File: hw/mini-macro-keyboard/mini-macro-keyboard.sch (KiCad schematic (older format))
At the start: 11 parts

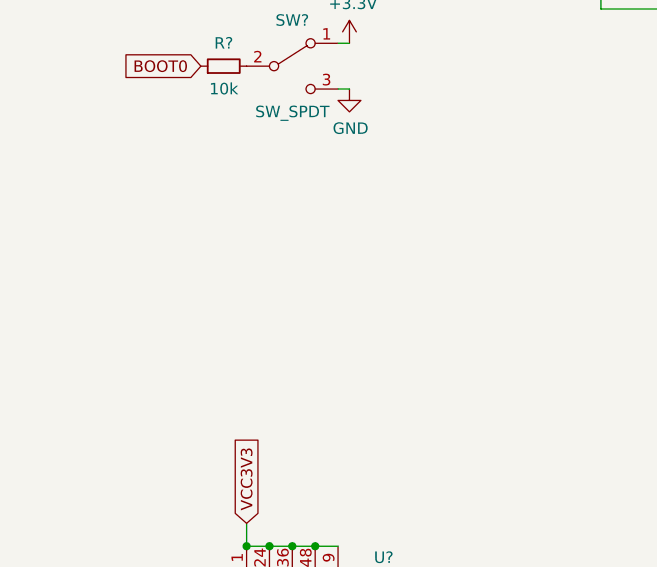
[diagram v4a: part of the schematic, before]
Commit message: feat(hw): add crystal to the schematic
Signed-off-by: Ivan Kovalenko <s1ckretbox@gmail.com>
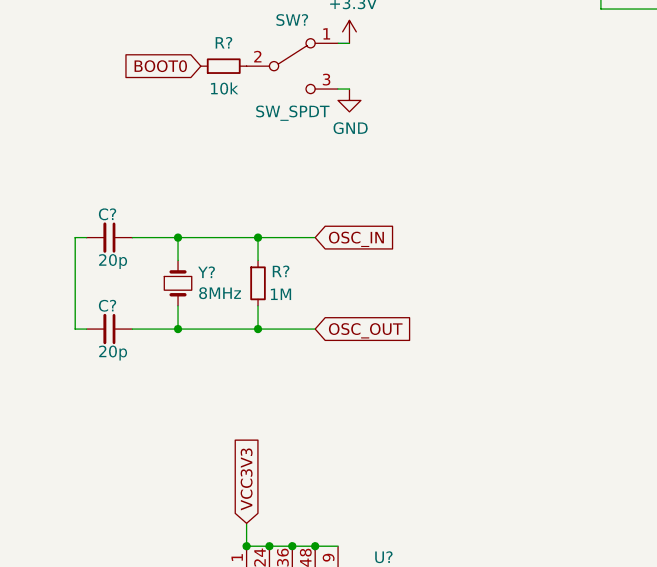
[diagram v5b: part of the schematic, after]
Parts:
- added C? (x2): 20p, symbol Device:C_Small
- added R?: 1M, symbol Device:R_Small
- added Y?: 8MHz, symbol Device:Crystal_Small
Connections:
- net OSC_IN: now also C?.1, R?.1, Y?.1
- net OSC_OUT: now also C?.1, R?.2, Y?.2
- new net: C?.2, C?.2
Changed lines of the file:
@@
 Text GLabel 3700 1200 1    50   Input ~ 0
 VCC3V3
-$Comp
-L Device:R_Small R?
-U 1 1 5FFE7355
-P 3700 1350
-F 0 "R?" V 3800 1350 50  0000 C CNN
-F 1 "10k" V 3600 1350 50  0000 C CNN
-F 2 "" H 3700 1350 50  0001 C CNN
-F 3 "~" H 3700 1350 50  0001 C CNN
-	1    3700 1350
-	1    0    0    -1
-$EndComp
 Wire Wire Line
 	3700 1250 3700 1200
@@
 Text GLabel 1200 4950 0    50   Input ~ 0
 OSC_IN
-Text GLabel 1200 5050 0    50   Input ~ 0
-OSC_OUT
 Text GLabel 2500 6950 2    50   Input ~ 0
 SWDIO
@@
 NoConn ~ 1200 5350
 NoConn ~ 1200 5250
+Text GLabel 1200 5050 0    50   Input ~ 0
+OSC_OUT
+$Comp
+L Device:Crystal_Small Y?
+U 1 1 6000CA22
+P 1400 3200
+F 0 "Y?" V 1354 3288 50  0000 L CNN
+F 1 "8MHz" V 1445 3288 50  0000 L CNN
+F 2 "" H 1400 3200 50  0001 C CNN
+F 3 "~" H 1400 3200 50  0001 C CNN
+	1    1400 3200
+	0    1    1    0
+$EndComp
+$Comp
+L Device:C_Small C?
+U 1 1 6000E4D6
+P 1100 3000
+F 0 "C?" V 1000 2950 50  0000 L CNN
+F 1 "20p" V 1200 2950 50  0000 L CNN
+F 2 "" H 1100 3000 50  0001 C CNN
+F 3 "~" H 1100 3000 50  0001 C CNN
+	1    1100 3000
+	0    1    1    0
+$EndComp
+$Comp
+L Device:C_Small C?
+U 1 1 6000EB9A
+P 1100 3400
+F 0 "C?" V 1000 3350 50  0000 L CNN
+F 1 "20p" V 1200 3350 50  0000 L CNN
+F 2 "" H 1100 3400 50  0001 C CNN
+F 3 "~" H 1100 3400 50  0001 C CNN
+	1    1100 3400
+	0    1    1    0
+$EndComp
+$Comp
+L Device:R_Small R?
+U 1 1 5FFE7355
+P 3700 1350
+F 0 "R?" V 3800 1350 50  0000 C CNN
+F 1 "10k" V 3600 1350 50  0000 C CNN
+F 2 "" H 3700 1350 50  0001 C CNN
+F 3 "~" H 3700 1350 50  0001 C CNN
+	1    3700 1350
+	1    0    0    -1
+$EndComp
+$Comp
+L Device:R_Small R?
+U 1 1 60011E97
+P 1750 3200
+F 0 "R?" H 1850 3250 50  0000 C CNN
+F 1 "1M" H 1850 3150 50  0000 C CNN
+F 2 "" H 1750 3200 50  0001 C CNN
+F 3 "~" H 1750 3200 50  0001 C CNN
+	1    1750 3200
+	1    0    0    -1
+$EndComp
+Wire Wire Line
+	1000 3000 950  3000
+Wire Wire Line
+	950  3000 950  3400
+Wire Wire Line
+	950  3400 1000 3400
+Wire Wire Line
+	1200 3000 1400 3000
+Wire Wire Line
+	1400 3000 1400 3100
+Wire Wire Line
+	1400 3300 1400 3400
+Wire Wire Line
+	1400 3400 1200 3400
+Connection ~ 1400 3000
+Connection ~ 1400 3400
+Text GLabel 2000 3000 2    50   Input ~ 0
+OSC_IN
+Text GLabel 2000 3400 2    50   Input ~ 0
+OSC_OUT
+Wire Wire Line
+	1400 3400 1750 3400
+Wire Wire Line
+	1400 3000 1750 3000
+Wire Wire Line
+	1750 3100 1750 3000
+Connection ~ 1750 3000
+Wire Wire Line
+	1750 3000 2000 3000
+Wire Wire Line
+	1750 3300 1750 3400
+Connection ~ 1750 3400
+Wire Wire Line
+	1750 3400 2000 3400
 $EndSCHEMATC

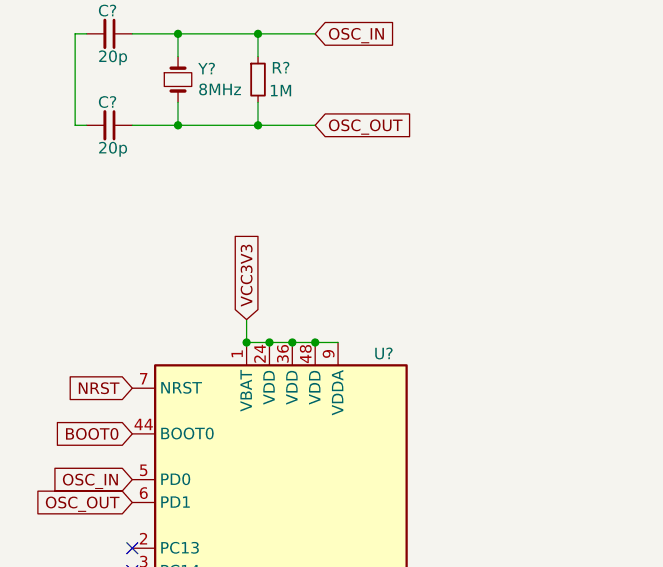
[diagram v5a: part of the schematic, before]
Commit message: fix(hw): remove VBAT connection
Signed-off-by: Ivan Kovalenko <s1ckretbox@gmail.com>
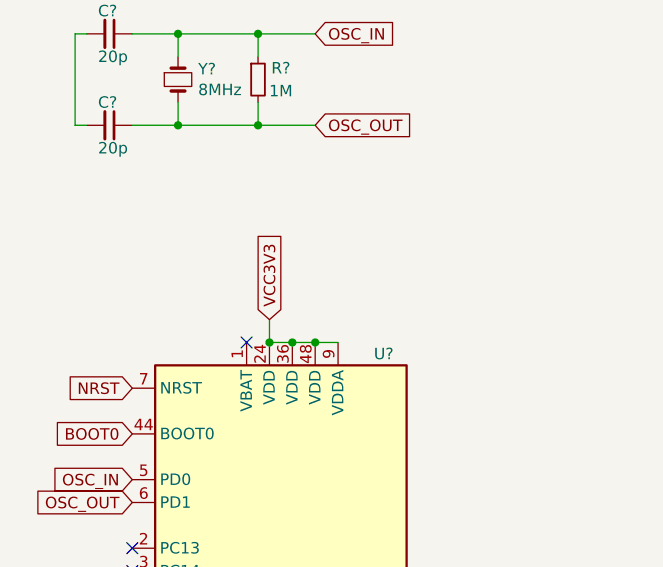
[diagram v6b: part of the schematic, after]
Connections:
- net +3V3: no longer U?.1 (VBAT)
- no-connect marks 24 -> 25
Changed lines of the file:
@@
 Wire Wire Line
 	1700 7350 1700 7450
-Text GLabel 1700 4250 1    50   Input ~ 0
+Text GLabel 1800 4250 1    50   Input ~ 0
 VCC3V3
 Text GLabel 1150 1100 0    50   Input ~ 0
 VCC3V3
-Wire Wire Line
-	1700 4250 1700 4350
 $Comp
 L Device:C_Small C?
@@
 	0    -1   -1   0
 $EndComp
-Connection ~ 1700 4350
 Connection ~ 2000 4350
 Wire Wire Line
@@
 	1900 4350 2000 4350
 Connection ~ 1900 4350
-Connection ~ 1800 4350
 Wire Wire Line
 	1800 4350 1900 4350
-Wire Wire Line
-	1700 4350 1800 4350
 Wire Wire Line
 	1900 7350 2000 7350
@@
 Wire Wire Line
 	1750 3400 2000 3400
+Wire Wire Line
+	1800 4250 1800 4350
+Connection ~ 1800 4350
+NoConn ~ 1700 4350
 $EndSCHEMATC

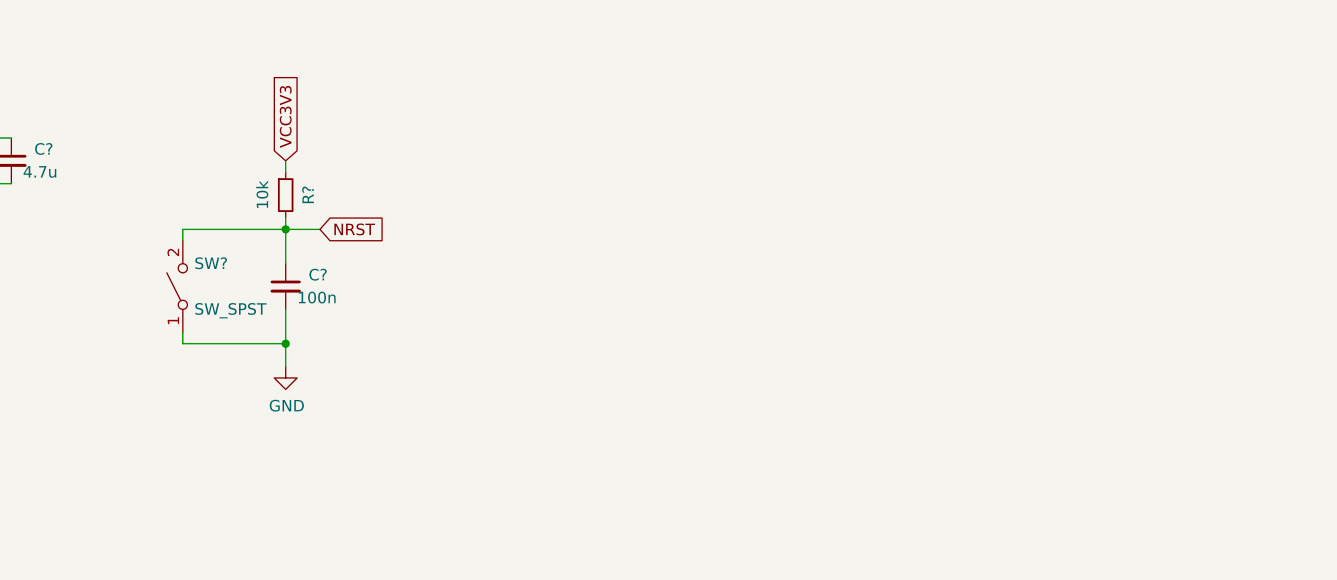
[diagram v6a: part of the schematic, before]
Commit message: feat(hw): add usblc6 protection
Signed-off-by: Ivan Kovalenko <s1ckretbox@gmail.com>
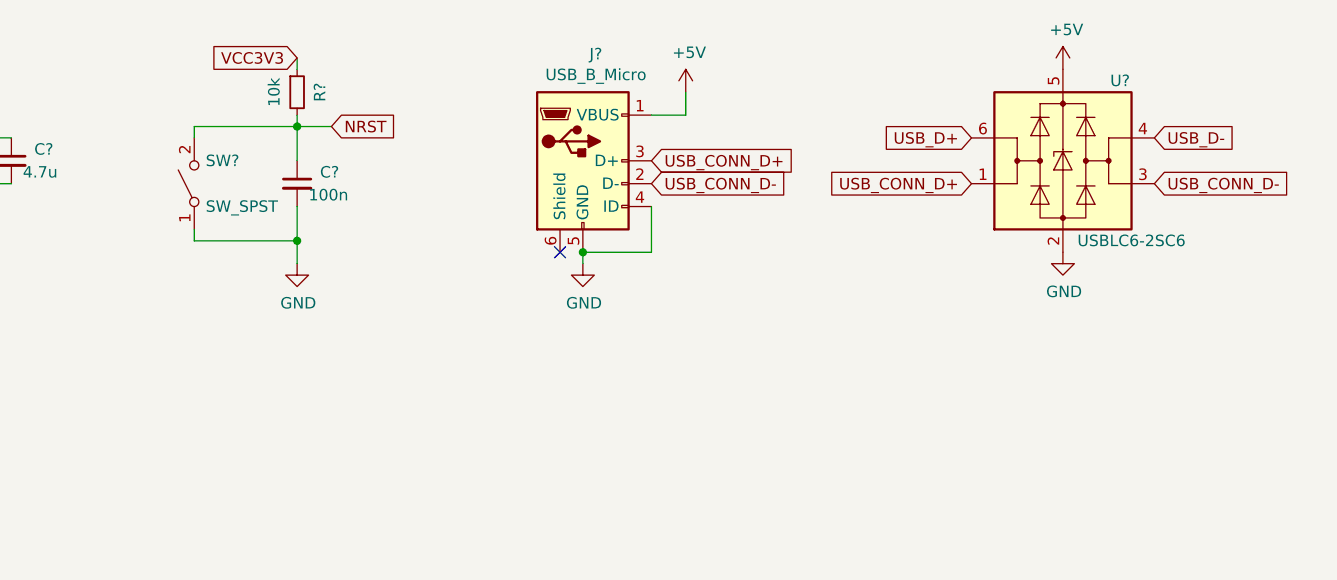
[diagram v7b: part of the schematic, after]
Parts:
- added J?: USB_B_Micro, symbol Connector:USB_B_Micro
- added U?: USBLC6-2SC6, Package_TO_SOT_SMD:SOT-23-6, symbol Power_Protection:USBLC6-2SC6
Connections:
- net GND: now also J?.4 (ID), J?.5 (GND), U?.2 (GND)
- net USB_D+: now also U?.6 (I/O1)
- net USB_D-: now also U?.4 (I/O2)
- new net +5V: J?.1 (VBUS), U?.5 (VBUS)
- new net USB_CONN_D+: J?.3 (D+), U?.1 (I/O1)
- new net USB_CONN_D-: J?.2 (D-), U?.3 (I/O2)
- no-connect marks 25 -> 26
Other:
- moved on the sheet: C?, R?, SW?
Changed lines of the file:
@@
 L Device:C_Small C?
 U 1 1 5FF9DDD1
-P 3700 1750
-F 0 "C?" H 3800 1800 50  0000 L CNN
-F 1 "100n" H 3750 1700 50  0000 L CNN
-F 2 "" H 3700 1750 50  0001 C CNN
-F 3 "~" H 3700 1750 50  0001 C CNN
-	1    3700 1750
+P 3750 1300
+F 0 "C?" H 3850 1350 50  0000 L CNN
+F 1 "100n" H 3800 1250 50  0000 L CNN
+F 2 "" H 3750 1300 50  0001 C CNN
+F 3 "~" H 3750 1300 50  0001 C CNN
+	1    3750 1300
 	1    0    0    -1
 $EndComp
@@
 Text GLabel 1200 4550 0    50   Input ~ 0
 NRST
-Text GLabel 3700 1200 1    50   Input ~ 0
+Text GLabel 3750 750  0    50   Input ~ 0
 VCC3V3
 Wire Wire Line
-	3700 1250 3700 1200
+	3750 800  3750 750
 $Comp
 L Switch:SW_SPST SW?
 U 1 1 5FFE8976
-P 3250 1750
-F 0 "SW?" V 3350 1700 50  0000 R CNN
-F 1 "SW_SPST" V 3150 1700 50  0000 R CNN
-F 2 "" H 3250 1750 50  0001 C CNN
-F 3 "~" H 3250 1750 50  0001 C CNN
-	1    3250 1750
+P 3300 1300
+F 0 "SW?" V 3400 1250 50  0000 R CNN
+F 1 "SW_SPST" V 3200 1250 50  0000 R CNN
+F 2 "" H 3300 1300 50  0001 C CNN
+F 3 "~" H 3300 1300 50  0001 C CNN
+	1    3300 1300
 	0    -1   -1   0
 $EndComp
 Wire Wire Line
-	3700 1450 3700 1500
-Wire Wire Line
-	3700 1500 3250 1500
-Wire Wire Line
-	3250 1500 3250 1550
+	3750 1000 3750 1050
+Wire Wire Line
+	3750 1050 3300 1050
+Wire Wire Line
+	3300 1050 3300 1100
 $Comp
 L power:GND #PWR?
 U 1 1 5FFEBFB1
-P 3700 2100
-F 0 "#PWR?" H 3700 1850 50  0001 C CNN
-F 1 "GND" H 3705 1927 50  0000 C CNN
-F 2 "" H 3700 2100 50  0001 C CNN
-F 3 "" H 3700 2100 50  0001 C CNN
-	1    3700 2100
-	1    0    0    -1
-$EndComp
-Wire Wire Line
-	3250 1950 3250 2000
-Wire Wire Line
-	3250 2000 3700 2000
-Wire Wire Line
-	3700 2000 3700 2100
-Wire Wire Line
-	3700 2000 3700 1850
-Connection ~ 3700 2000
-Wire Wire Line
-	3700 1650 3700 1500
-Connection ~ 3700 1500
-Text GLabel 3850 1500 2    50   Input ~ 0
+P 3750 1650
+F 0 "#PWR?" H 3750 1400 50  0001 C CNN
+F 1 "GND" H 3755 1477 50  0000 C CNN
+F 2 "" H 3750 1650 50  0001 C CNN
+F 3 "" H 3750 1650 50  0001 C CNN
+	1    3750 1650
+	1    0    0    -1
+$EndComp
+Wire Wire Line
+	3300 1500 3300 1550
+Wire Wire Line
+	3300 1550 3750 1550
+Wire Wire Line
+	3750 1550 3750 1650
+Wire Wire Line
+	3750 1550 3750 1400
+Connection ~ 3750 1550
+Wire Wire Line
+	3750 1200 3750 1050
+Connection ~ 3750 1050
+Text GLabel 3900 1050 2    50   Input ~ 0
 NRST
 Wire Wire Line
-	3700 1500 3850 1500
+	3750 1050 3900 1050
 Text GLabel 1200 4950 0    50   Input ~ 0
 OSC_IN
@@
 L Device:R_Small R?
 U 1 1 5FFE7355
-P 3700 1350
-F 0 "R?" V 3800 1350 50  0000 C CNN
-F 1 "10k" V 3600 1350 50  0000 C CNN
-F 2 "" H 3700 1350 50  0001 C CNN
-F 3 "~" H 3700 1350 50  0001 C CNN
-	1    3700 1350
+P 3750 900
+F 0 "R?" V 3850 900 50  0000 C CNN
+F 1 "10k" V 3650 900 50  0000 C CNN
+F 2 "" H 3750 900 50  0001 C CNN
+F 3 "~" H 3750 900 50  0001 C CNN
+	1    3750 900
 	1    0    0    -1
 $EndComp
@@
 Connection ~ 1800 4350
 NoConn ~ 1700 4350
+$Comp
+L Connector:USB_B_Micro J?
+U 1 1 6001BB49
+P 5000 1200
+F 0 "J?" H 5057 1667 50  0000 C CNN
+F 1 "USB_B_Micro" H 5057 1576 50  0000 C CNN
+F 2 "" H 5150 1150 50  0001 C CNN
+F 3 "~" H 5150 1150 50  0001 C CNN
+	1    5000 1200
+	1    0    0    -1
+$EndComp
+$Comp
+L power:GND #PWR?
+U 1 1 60020BF2
+P 5000 1650
+F 0 "#PWR?" H 5000 1400 50  0001 C CNN
+F 1 "GND" H 5005 1477 50  0000 C CNN
+F 2 "" H 5000 1650 50  0001 C CNN
+F 3 "" H 5000 1650 50  0001 C CNN
+	1    5000 1650
+	1    0    0    -1
+$EndComp
+NoConn ~ 4900 1600
+Wire Wire Line
+	5300 1400 5300 1600
+Wire Wire Line
+	5300 1600 5000 1600
+Connection ~ 5000 1600
+Wire Wire Line
+	5000 1600 5000 1650
+$Comp
+L power:+5V #PWR?
+U 1 1 60024143
+P 5450 900
+F 0 "#PWR?" H 5450 750 50  0001 C CNN
+F 1 "+5V" H 5465 1073 50  0000 C CNN
+F 2 "" H 5450 900 50  0001 C CNN
+F 3 "" H 5450 900 50  0001 C CNN
+	1    5450 900
+	1    0    0    -1
+$EndComp
+Wire Wire Line
+	5450 900  5450 1000
+Wire Wire Line
+	5450 1000 5300 1000
+$Comp
+L Power_Protection:USBLC6-2SC6 U?
+U 1 1 60025D65
+P 7100 1200
+F 0 "U?" H 7350 1550 50  0000 C CNN
+F 1 "USBLC6-2SC6" H 7400 850 50  0000 C CNN
+F 2 "Package_TO_SOT_SMD:SOT-23-6" H 7100 700 50  0001 C CNN
+F 3 "https://www.st.com/resource/en/datasheet/usblc6-2.pdf" H 7300 1550 50  0001 C CNN
+	1    7100 1200
+	1    0    0    -1
+$EndComp
+Text GLabel 5300 1200 2    50   Input ~ 0
+USB_CONN_D+
+Text GLabel 5300 1300 2    50   Input ~ 0
+USB_CONN_D-
+Text GLabel 6700 1300 0    50   Input ~ 0
+USB_CONN_D+
+$Comp
+L power:+5V #PWR?
+U 1 1 6002EBC6
+P 7100 800
+F 0 "#PWR?" H 7100 650 50  0001 C CNN
+F 1 "+5V" H 7115 973 50  0000 C CNN
+F 2 "" H 7100 800 50  0001 C CNN
+F 3 "" H 7100 800 50  0001 C CNN
+	1    7100 800
+	1    0    0    -1
+$EndComp
+$Comp
+L power:GND #PWR?
+U 1 1 6002F1AC
+P 7100 1600
+F 0 "#PWR?" H 7100 1350 50  0001 C CNN
+F 1 "GND" H 7105 1427 50  0000 C CNN
+F 2 "" H 7100 1600 50  0001 C CNN
+F 3 "" H 7100 1600 50  0001 C CNN
+	1    7100 1600
+	1    0    0    -1
+$EndComp
+Text GLabel 6700 1100 0    50   Input ~ 0
+USB_D+
+Text GLabel 7500 1300 2    50   Input ~ 0
+USB_CONN_D-
+Text GLabel 7500 1100 2    50   Input ~ 0
+USB_D-
 $EndSCHEMATC
